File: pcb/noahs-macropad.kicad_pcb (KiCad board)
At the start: 2 copper layers, 99 x 39 mm, 17 parts, among them U1 MOUDLE-SEEEDUINO-XIAO

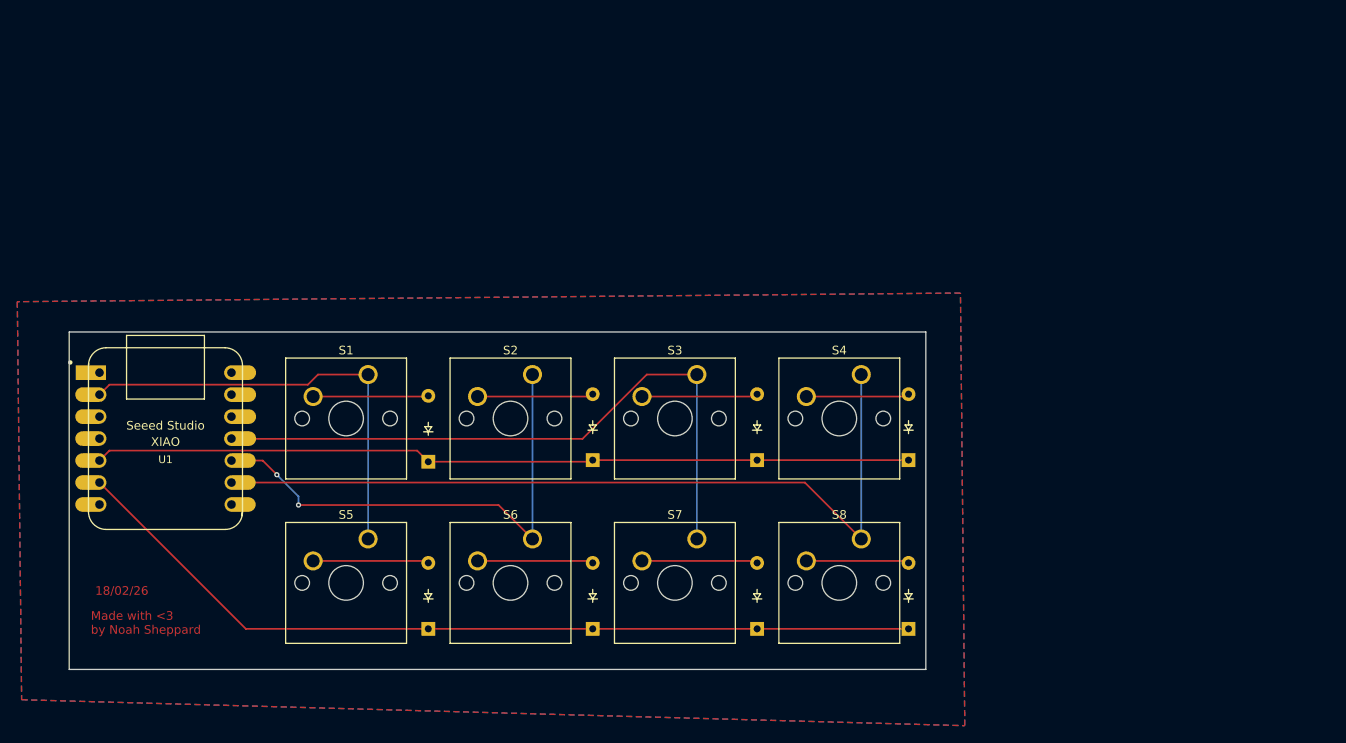
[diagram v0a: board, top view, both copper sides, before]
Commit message: redesign with oled screen
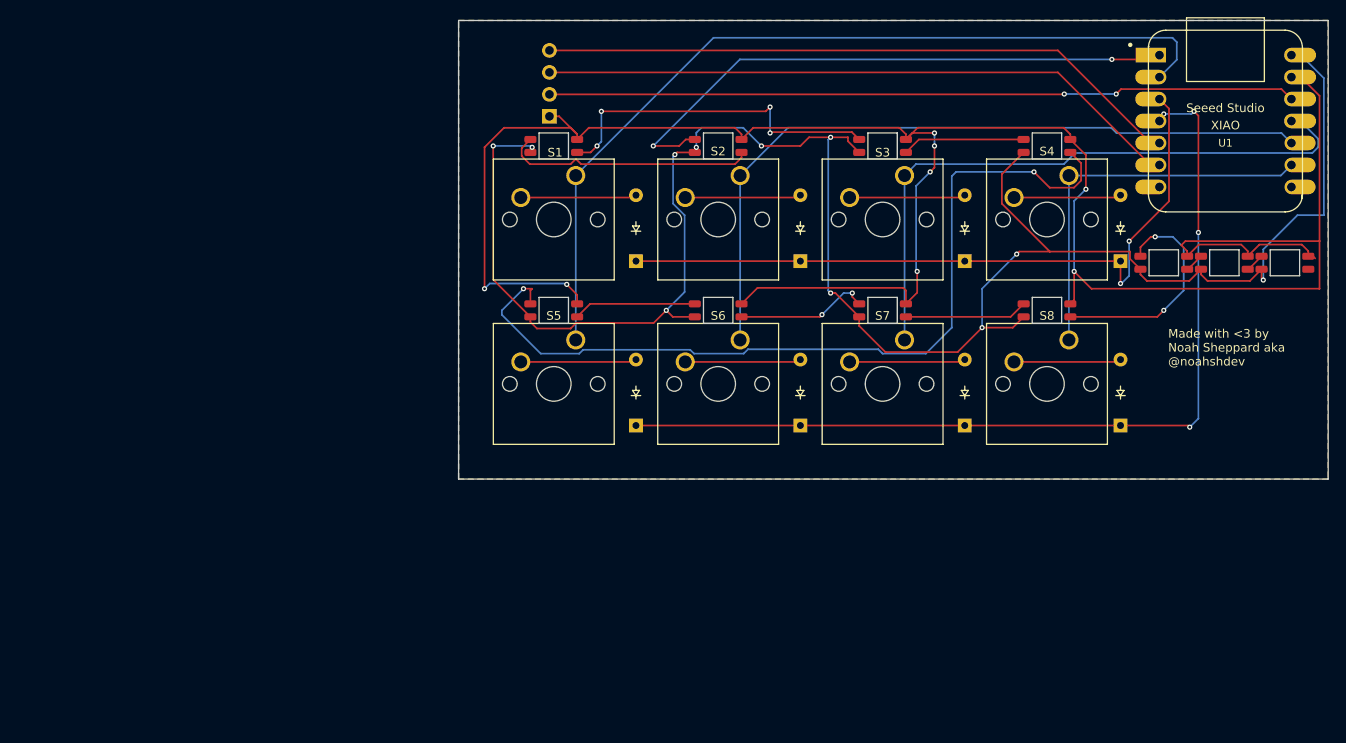
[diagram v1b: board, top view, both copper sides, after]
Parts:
- added D10: LED_SK6812MINI, ScottoKeebs_Components:LED_SK6812MINI, F.Cu at (102.5, 78.0)
- added D11: LED_SK6812MINI, ScottoKeebs_Components:LED_SK6812MINI, F.Cu at (121.5, 78.0)
- added D12: LED_SK6812MINI, ScottoKeebs_Components:LED_SK6812MINI, F.Cu at (140.5, 78.0)
- added D13: LED_SK6812MINI, ScottoKeebs_Components:LED_SK6812MINI, F.Cu at (83.5, 97.0)
- added D14: LED_SK6812MINI, ScottoKeebs_Components:LED_SK6812MINI, F.Cu at (102.5, 97.0)
- added D15: LED_SK6812MINI, ScottoKeebs_Components:LED_SK6812MINI, F.Cu at (121.5, 97.0)
- added D16: LED_SK6812MINI, ScottoKeebs_Components:LED_SK6812MINI, F.Cu at (140.5, 97.0)
- added D17: LED_SK6812MINI, ScottoKeebs_Components:LED_SK6812MINI, F.Cu at (154.0, 91.5)
- added D18: LED_SK6812MINI, ScottoKeebs_Components:LED_SK6812MINI, F.Cu at (161.0, 91.5)
- added D19: LED_SK6812MINI, ScottoKeebs_Components:LED_SK6812MINI, F.Cu at (168.0, 91.5)
- added D9: LED_SK6812MINI, ScottoKeebs_Components:LED_SK6812MINI, F.Cu at (83.5, 78.0)
- added J1: OLED_128x32, ScottoKeebs_Components:OLED_128x32, F.Cu at (81.4, 64.8)
- moved U1 127.9 mm to (161.1, 75.1)
- moved D8 33.9 mm to (149.0, 110.3)
- moved D4 33.6 mm to (149.0, 91.3)
- moved D5 33.6 mm to (93.0, 110.3)
- moved D6 33.6 mm to (112.0, 110.3)
- moved D7 33.6 mm to (131.0, 110.3)
- moved D1 33.4 mm to (93.0, 91.3)
- moved S1 33.2 mm to (86.0, 81.4)
- moved S5 33.2 mm to (86.0, 100.4)
- moved D2 33.2 mm to (112.0, 91.3)
- moved D3 33.2 mm to (131.0, 91.3)
- moved S2 33.2 mm to (105.0, 81.4)
- moved S3 33.2 mm to (124.0, 81.4)
- moved S6 33.2 mm to (105.0, 100.4)
- moved S7 33.2 mm to (124.0, 100.4)
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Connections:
- U1 pad 1: unconnected-(U1-PA02_A0_D0-Pad1) -> LED0_DIN
- U1 pad 12: unconnected-(U1-3V3-Pad12) -> OLED_VCC
- U1 pad 13: GND -> LED_GND
- U1 pad 14: unconnected-(U1-5V-Pad14) -> 5V
- U1 pad 3: unconnected-(U1-PA10_A2_D2-Pad3) -> Row 0
- U1 pad 4: unconnected-(U1-PA11_A3_D3-Pad4) -> Row 1
- U1 pad 5: Row 0 -> OLED_SDA
- U1 pad 6: Row 1 -> OLED_SCL
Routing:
- net LED_GND: track 0.00 -> 264.9 mm, vias 0 -> 8
- net 5V: track 0.00 -> 231.0 mm, vias 0 -> 11
- net Net-(D12-DOUT): track 0.00 -> 100.3 mm, vias 0 -> 2
- net OLED_VCC: track 0.00 -> 86.5 mm, vias 0 -> 2
- net OLED_SDA: track 0.00 -> 74.9 mm
- net OLED_SCL: track 0.00 -> 74.9 mm
- net LED0_DIN: track 0.00 -> 68.0 mm, vias 0 -> 2
- net Col 3: track 94.5 -> 45.2 mm
- net Col 0: track 51.0 -> 100.1 mm
- net Net-(D11-DIN): track 0.00 -> 40.2 mm, vias 0 -> 4
- net Net-(D10-DOUT): track 0.00 -> 29.5 mm
- net Col 1: track 58.1 -> 85.7 mm, vias 2 -> 0
- net Net-(D16-DOUT): track 0.00 -> 26.4 mm, vias 0 -> 2
- net Net-(D14-DOUT): track 0.00 -> 15.5 mm, vias 0 -> 2
- net Net-(D15-DOUT): track 0.00 -> 14.2 mm
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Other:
- board size 99 x 39 mm -> 100.5 x 53 mm
- board text added: "Made with <3 by Noah Sheppard aka @noahshdev"
- board text removed: "18/02/26"
- board text removed: "Made with <3 by Noah Sheppard"
